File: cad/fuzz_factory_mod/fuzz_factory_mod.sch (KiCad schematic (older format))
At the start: 0 parts

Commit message: Continued schematic
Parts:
- added NT? (x2): Net-Tie_2, symbol Device:Net-Tie_2
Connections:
- new net GNDA: NT?.1
- new net GNDD: NT?.2
- new net GNDPWR: NT?.1, NT?.2
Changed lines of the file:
@@
 $Descr A4 11693 8268
 encoding utf-8
-Sheet 1 5
+Sheet 1 6
 Title ""
 Date ""
@@
 F1 "connectors.sch" 50
 $EndSheet
+$Comp
+L power:GNDA #PWR?
+U 1 1 5E05A512
+P 9000 6000
+F 0 "#PWR?" H 9000 5750 50  0001 C CNN
+F 1 "GNDA" H 9005 5827 50  0000 C CNN
+F 2 "" H 9000 6000 50  0001 C CNN
+F 3 "" H 9000 6000 50  0001 C CNN
+	1    9000 6000
+	1    0    0    -1
+$EndComp
+$Comp
+L power:GNDPWR #PWR?
+U 1 1 5E05AF8B
+P 9500 6000
+F 0 "#PWR?" H 9500 5800 50  0001 C CNN
+F 1 "GNDPWR" H 9504 5846 50  0000 C CNN
+F 2 "" H 9500 5950 50  0001 C CNN
+F 3 "" H 9500 5950 50  0001 C CNN
+	1    9500 6000
+	1    0    0    -1
+$EndComp
+$Comp
+L power:GNDD #PWR?
+U 1 1 5E05B768
+P 10000 6000
+F 0 "#PWR?" H 10000 5750 50  0001 C CNN
+F 1 "GNDD" H 10004 5845 50  0000 C CNN
+F 2 "" H 10000 6000 50  0001 C CNN
+F 3 "" H 10000 6000 50  0001 C CNN
+	1    10000 6000
+	1    0    0    -1
+$EndComp
+$Comp
+L Device:Net-Tie_2 NT?
+U 1 1 5E05BC9C
+P 9250 5800
+F 0 "NT?" H 9250 5981 50  0000 C CNN
+F 1 "Net-Tie_2" H 9250 5890 50  0000 C CNN
+F 2 "" H 9250 5800 50  0001 C CNN
+F 3 "~" H 9250 5800 50  0001 C CNN
+	1    9250 5800
+	1    0    0    -1
+$EndComp
+$Comp
+L Device:Net-Tie_2 NT?
+U 1 1 5E05C2E4
+P 9750 5800
+F 0 "NT?" H 9750 5981 50  0000 C CNN
+F 1 "Net-Tie_2" H 9750 5890 50  0000 C CNN
+F 2 "" H 9750 5800 50  0001 C CNN
+F 3 "~" H 9750 5800 50  0001 C CNN
+	1    9750 5800
+	1    0    0    -1
+$EndComp
+Wire Wire Line
+	10000 6000 10000 5800
+Wire Wire Line
+	10000 5800 9850 5800
+Wire Wire Line
+	9650 5800 9500 5800
+Wire Wire Line
+	9500 6000 9500 5800
+Connection ~ 9500 5800
+Wire Wire Line
+	9500 5800 9350 5800
+Wire Wire Line
+	9000 6000 9000 5800
+Wire Wire Line
+	9000 5800 9150 5800
 $EndSCHEMATC

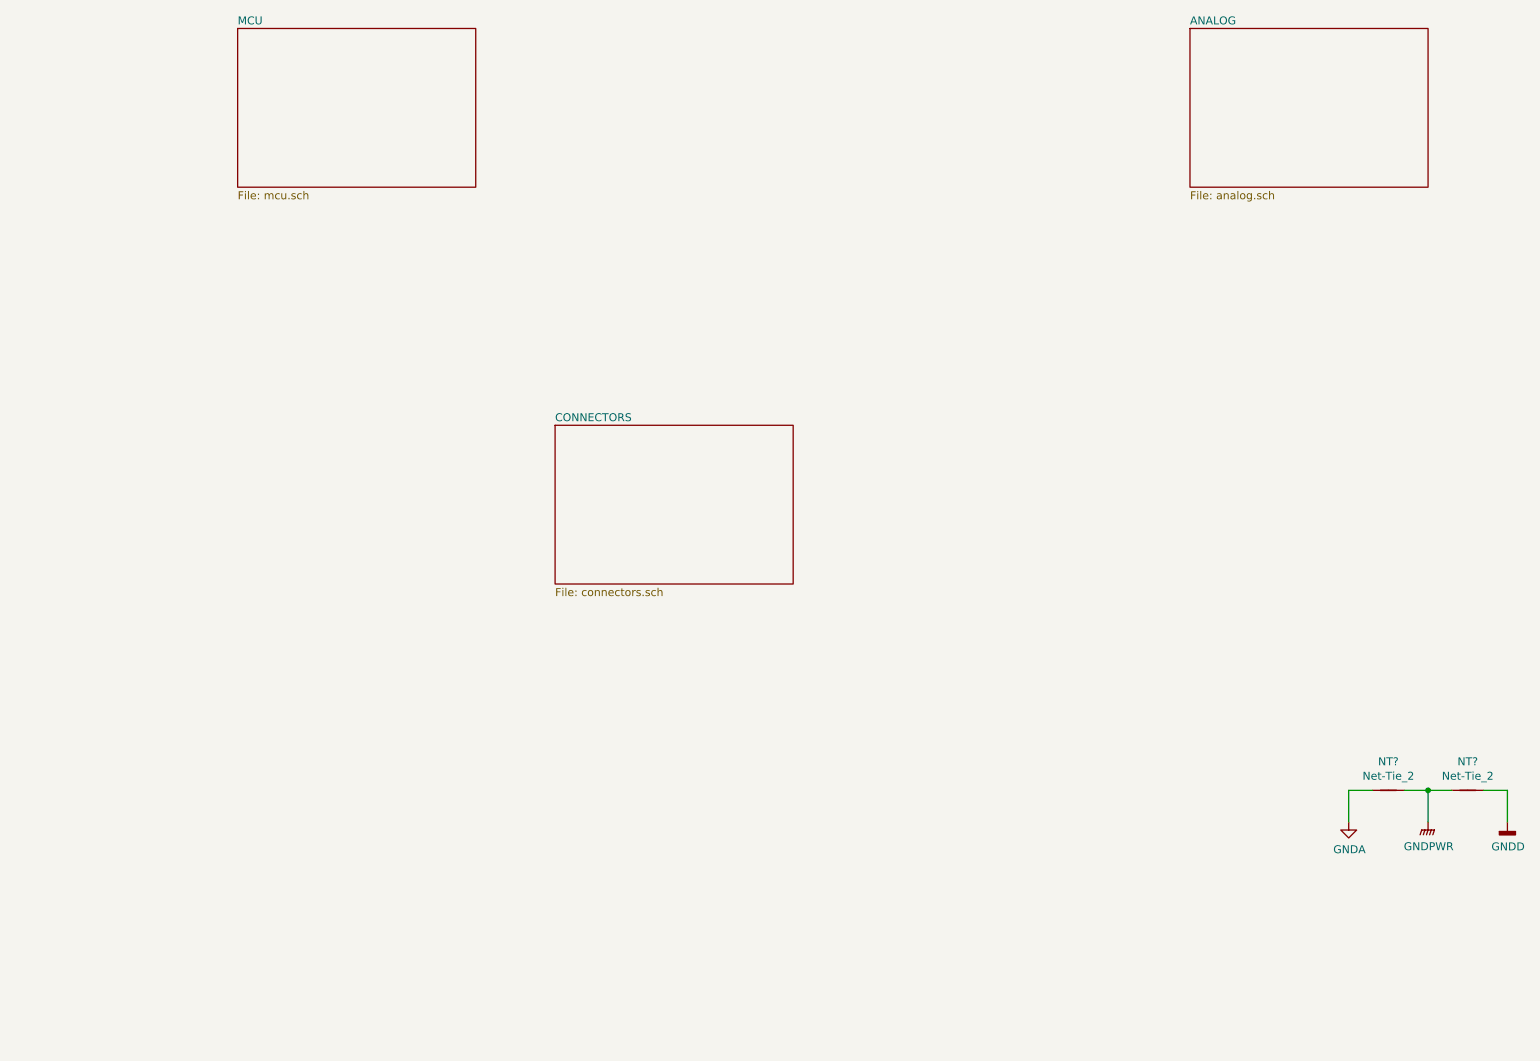
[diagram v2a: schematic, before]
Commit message: Continued schematic.
Added PSU and interface from tremolo project.
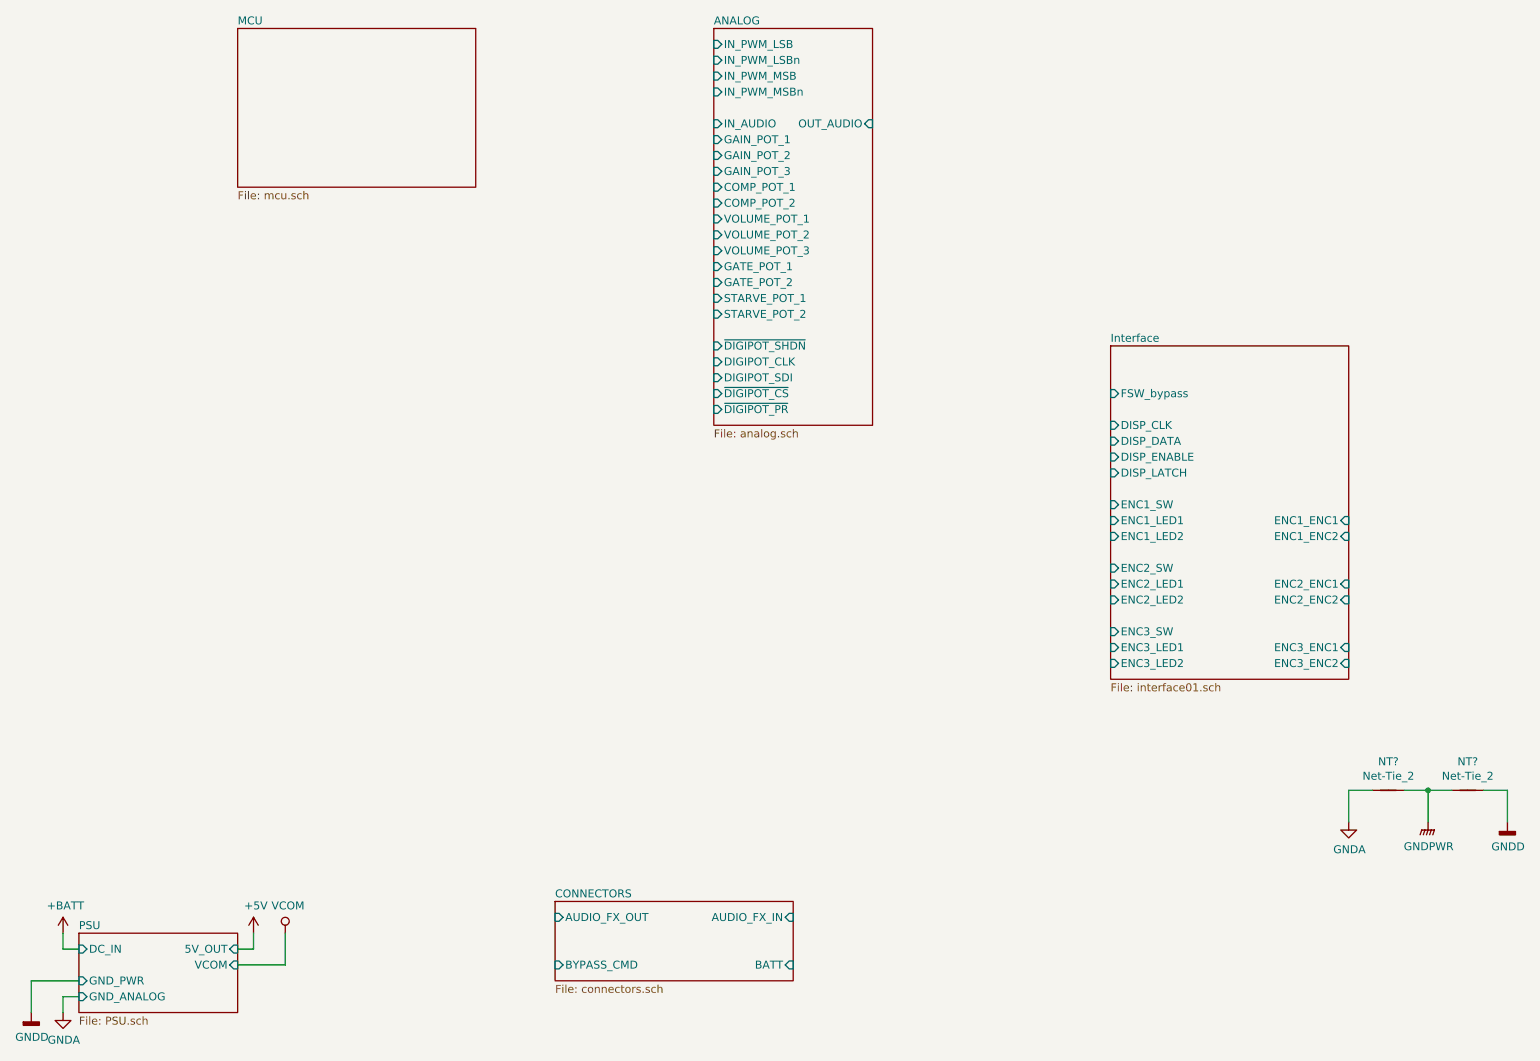
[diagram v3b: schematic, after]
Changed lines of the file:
@@
 $Descr A4 11693 8268
 encoding utf-8
-Sheet 1 6
+Sheet 1 11
 Title ""
 Date ""
@@
 $EndSheet
 $Sheet
-S 8000 1000 1500 1000
+S 5000 1000 1000 2500
 U 5DE4AD88
 F0 "ANALOG" 50
 F1 "analog.sch" 50
-$EndSheet
-$Sheet
-S 4000 3500 1500 1000
+F2 "GAIN_POT_1" I L 5000 1700 50
+F3 "GAIN_POT_2" I L 5000 1800 50
+F4 "GAIN_POT_3" I L 5000 1900 50
+F5 "COMP_POT_1" I L 5000 2000 50
+F6 "COMP_POT_2" I L 5000 2100 50
+F7 "VOLUME_POT_1" I L 5000 2200 50
+F8 "VOLUME_POT_2" I L 5000 2300 50
+F9 "VOLUME_POT_3" I L 5000 2400 50
+F10 "GATE_POT_1" I L 5000 2500 50
+F11 "GATE_POT_2" I L 5000 2600 50
+F12 "IN_AUDIO" I L 5000 1600 50
+F13 "IN_PWM_LSB" I L 5000 1100 50
+F14 "IN_PWM_LSBn" I L 5000 1200 50
+F15 "IN_PWM_MSB" I L 5000 1300 50
+F16 "IN_PWM_MSBn" I L 5000 1400 50
+F17 "STARVE_POT_1" I L 5000 2700 50
+F18 "STARVE_POT_2" I L 5000 2800 50
+F19 "OUT_AUDIO" I R 6000 1600 50
+F20 "~DIGIPOT_SHDN" I L 5000 3000 50
+F21 "DIGIPOT_CLK" I L 5000 3100 50
+F22 "DIGIPOT_SDI" I L 5000 3200 50
+F23 "~DIGIPOT_CS" I L 5000 3300 50
+F24 "~DIGIPOT_PR" I L 5000 3400 50
+$EndSheet
+$Sheet
+S 4000 6500 1500 500
 U 5DE5A177
 F0 "CONNECTORS" 50
 F1 "connectors.sch" 50
+F2 "BYPASS_CMD" I L 4000 6900 50
+F3 "AUDIO_FX_IN" I R 5500 6600 50
+F4 "AUDIO_FX_OUT" I L 4000 6600 50
+F5 "BATT" I R 5500 6900 50
 $EndSheet
 $Comp
@@
 Wire Wire Line
 	9000 5800 9150 5800
+$Sheet
+S 7500 3000 1500 2100
+U 5E083283
+F0 "Interface" 50
+F1 "interface01.sch" 50
+F2 "DISP_CLK" I L 7500 3500 50
+F3 "DISP_DATA" I L 7500 3600 50
+F4 "DISP_ENABLE" I L 7500 3700 50
+F5 "DISP_LATCH" I L 7500 3800 50
+F6 "ENC1_SW" I L 7500 4000 50
+F7 "ENC1_LED1" I L 7500 4100 50
+F8 "ENC1_LED2" I L 7500 4200 50
+F9 "ENC1_ENC1" I R 9000 4100 50
+F10 "ENC1_ENC2" I R 9000 4200 50
+F11 "FSW_bypass" I L 7500 3300 50
+F12 "ENC2_SW" I L 7500 4400 50
+F13 "ENC2_LED1" I L 7500 4500 50
+F14 "ENC2_LED2" I L 7500 4600 50
+F15 "ENC2_ENC1" I R 9000 4500 50
+F16 "ENC2_ENC2" I R 9000 4600 50
+F17 "ENC3_SW" I L 7500 4800 50
+F18 "ENC3_LED1" I L 7500 4900 50
+F19 "ENC3_LED2" I L 7500 5000 50
+F20 "ENC3_ENC1" I R 9000 4900 50
+F21 "ENC3_ENC2" I R 9000 5000 50
+$EndSheet
+$Sheet
+S 1000 6700 1000 500
+U 5E2FAB43
+F0 "PSU" 50
+F1 "PSU.sch" 50
+F2 "DC_IN" I L 1000 6800 50
+F3 "GND_PWR" I L 1000 7000 50
+F4 "5V_OUT" I R 2000 6800 50
+F5 "VCOM" I R 2000 6900 50
+F6 "GND_ANALOG" I L 1000 7100 50
+$EndSheet
+$Comp
+L power:+5V #PWR?
+U 1 1 5E32C912
+P 2100 6700
+F 0 "#PWR?" H 2100 6550 50  0001 C CNN
+F 1 "+5V" H 2115 6873 50  0000 C CNN
+F 2 "" H 2100 6700 50  0001 C CNN
+F 3 "" H 2100 6700 50  0001 C CNN
+	1    2100 6700
+	1    0    0    -1
+$EndComp
+$Comp
+L power:VCOM #PWR?
+U 1 1 5E32D8FB
+P 2300 6700
+F 0 "#PWR?" H 2300 6550 50  0001 C CNN
+F 1 "VCOM" H 2317 6873 50  0000 C CNN
+F 2 "" H 2300 6700 50  0001 C CNN
+F 3 "" H 2300 6700 50  0001 C CNN
+	1    2300 6700
+	1    0    0    -1
+$EndComp
+Wire Wire Line
+	2100 6700 2100 6800
+Wire Wire Line
+	2100 6800 2000 6800
+Wire Wire Line
+	2000 6900 2300 6900
+Wire Wire Line
+	2300 6900 2300 6700
+$Comp
+L power:GNDD #PWR?
+U 1 1 5E32E854
+P 700 7200
+F 0 "#PWR?" H 700 6950 50  0001 C CNN
+F 1 "GNDD" H 704 7045 50  0000 C CNN
+F 2 "" H 700 7200 50  0001 C CNN
+F 3 "" H 700 7200 50  0001 C CNN
+	1    700  7200
+	1    0    0    -1
+$EndComp
+$Comp
+L power:GNDA #PWR?
+U 1 1 5E330132
+P 900 7200
+F 0 "#PWR?" H 900 6950 50  0001 C CNN
+F 1 "GNDA" H 905 7027 50  0000 C CNN
+F 2 "" H 900 7200 50  0001 C CNN
+F 3 "" H 900 7200 50  0001 C CNN
+	1    900  7200
+	1    0    0    -1
+$EndComp
+Wire Wire Line
+	900  7200 900  7100
+Wire Wire Line
+	900  7100 1000 7100
+Wire Wire Line
+	1000 7000 700  7000
+Wire Wire Line
+	700  7000 700  7200
+$Comp
+L power:+BATT #PWR?
+U 1 1 5E3312DB
+P 900 6700
+F 0 "#PWR?" H 900 6550 50  0001 C CNN
+F 1 "+BATT" H 915 6873 50  0000 C CNN
+F 2 "" H 900 6700 50  0001 C CNN
+F 3 "" H 900 6700 50  0001 C CNN
+	1    900  6700
+	1    0    0    -1
+$EndComp
+Wire Wire Line
+	900  6700 900  6800
+Wire Wire Line
+	900  6800 1000 6800
 $EndSCHEMATC

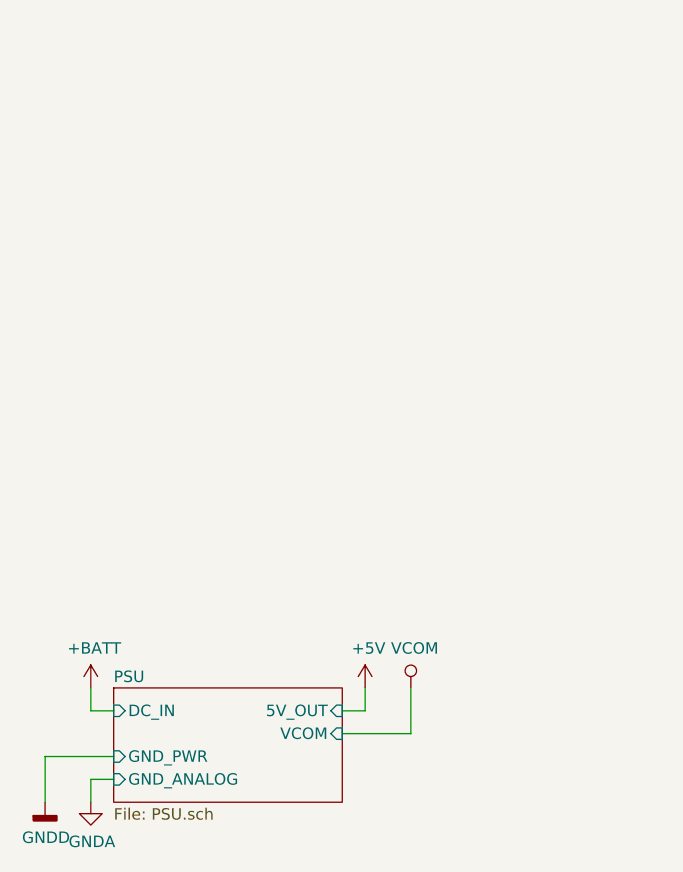
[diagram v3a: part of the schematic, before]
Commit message: Factorised fuzz factory circuit.
Added MIDI interface.
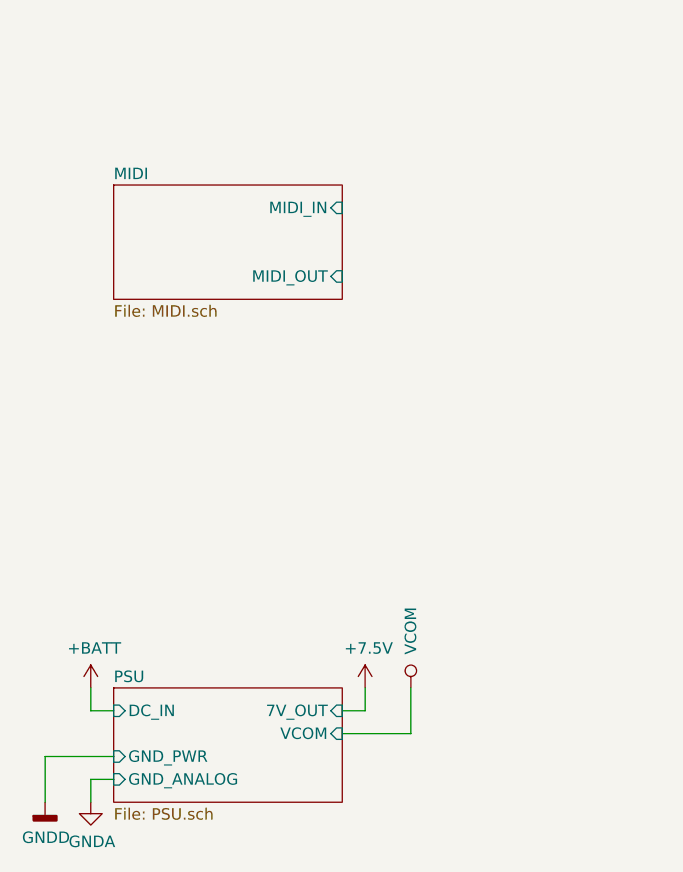
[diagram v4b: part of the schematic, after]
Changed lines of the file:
@@
 $Descr A4 11693 8268
 encoding utf-8
-Sheet 1 11
+Sheet 1 14
 Title ""
 Date ""
@@
 F2 "DC_IN" I L 1000 6800 50
 F3 "GND_PWR" I L 1000 7000 50
-F4 "5V_OUT" I R 2000 6800 50
-F5 "VCOM" I R 2000 6900 50
-F6 "GND_ANALOG" I L 1000 7100 50
-$EndSheet
-$Comp
-L power:+5V #PWR?
-U 1 1 5E32C912
-P 2100 6700
-F 0 "#PWR?" H 2100 6550 50  0001 C CNN
-F 1 "+5V" H 2115 6873 50  0000 C CNN
-F 2 "" H 2100 6700 50  0001 C CNN
-F 3 "" H 2100 6700 50  0001 C CNN
-	1    2100 6700
-	1    0    0    -1
-$EndComp
+F4 "VCOM" I R 2000 6900 50
+F5 "GND_ANALOG" I L 1000 7100 50
+F6 "7V_OUT" I R 2000 6800 50
+$EndSheet
 $Comp
 L power:VCOM #PWR?
@@
 P 2300 6700
 F 0 "#PWR?" H 2300 6550 50  0001 C CNN
-F 1 "VCOM" H 2317 6873 50  0000 C CNN
+F 1 "VCOM" V 2300 6950 50  0000 C CNN
 F 2 "" H 2300 6700 50  0001 C CNN
 F 3 "" H 2300 6700 50  0001 C CNN
@@
 Wire Wire Line
 	900  6800 1000 6800
+$Comp
+L power:+7.5V #PWR?
+U 1 1 5E6791DE
+P 2100 6700
+F 0 "#PWR?" H 2100 6550 50  0001 C CNN
+F 1 "+7.5V" H 2115 6873 50  0000 C CNN
+F 2 "" H 2100 6700 50  0001 C CNN
+F 3 "" H 2100 6700 50  0001 C CNN
+	1    2100 6700
+	1    0    0    -1
+$EndComp
+$Sheet
+S 1000 4500 1000 500
+U 5E67C282
+F0 "MIDI" 50
+F1 "MIDI.sch" 50
+F2 "MIDI_IN" I R 2000 4600 50
+F3 "MIDI_OUT" I R 2000 4900 50
+$EndSheet
 $EndSCHEMATC
